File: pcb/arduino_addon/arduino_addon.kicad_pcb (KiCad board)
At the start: 2 copper layers, 100 x 53 mm, 32 parts, among them P1 AnalogIn, P11 ADC-DO, P12 ADC-DO, P13 ADC-DO, P14 ADC-DO, P15 DO, P16 3V3 ADC REF, P2 Power, P3 Digital1, P4 Digital2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

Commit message: adaq initial version, board design: extra bnc connector added
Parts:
- added P17: BNC, rzfp:bnc, F.Cu at (172.0, 113.0)
- P15: footprint Pin_Headers:Pin_Header_Straight_1x05 -> Pin_Headers:Pin_Header_Straight_1x06
- moved D1 29.0 mm to (197.5, 103.2), turned to 180 degrees
- moved R1 7.25 mm to (186.0, 103.2), turned to 0 degrees
- moved C4 6.50 mm to (179.2, 124.2)
- moved R11 6.36 mm to (193.0, 117.2)
- moved P9 5.30 mm to (168.2, 125.2)
- moved R10 4.91 mm to (156.5, 123.2)
- moved R12 4.32 mm to (193.0, 124.2)
- moved R9 3.35 mm to (140.2, 122.5), turned to 180 degrees
- moved P15 2.55 mm to (154.8, 107.5)
- moved C3 0.79 mm to (151.8, 117.0)
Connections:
- P15 pad 1: /D4 -> +3V3
- P15 pad 2: /D5 -> /D4
- P15 pad 3: /D6 -> /D5
- P15 pad 4: /D7 -> /D6
- P15 pad 5: GND -> /D7
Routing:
- net (no net): track 611.8 -> 0.00 mm
- net GND: track 398.9 -> 449.0 mm, vias 5 -> 8
- net +3V3: track 127.2 -> 173.1 mm, vias 1 -> 7
- net /D4: track 5.54 -> 31.9 mm, vias 0 -> 1
- net /AD0: track 42.2 -> 56.6 mm, vias 1 -> 2
- net /D1: track 74.4 -> 63.0 mm, vias 1 -> 2
- net Net-(C3-Pad1): track 33.0 -> 43.5 mm
- net /D8: track 82.6 -> 89.8 mm
- net Net-(R10-Pad1): track 22.4 -> 15.8 mm, vias 1 -> 0
- net /DAC0: track 36.9 -> 30.7 mm
- net /AD2: track 23.6 -> 29.7 mm, vias 0 -> 2
- net /AI2: track 29.8 -> 25.6 mm
- net /D3: track 45.1 -> 48.6 mm
- net Net-(R11-Pad1): track 41.4 -> 44.6 mm
- net /D2: track 54.2 -> 57.1 mm, vias 1 -> 2
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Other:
- net class Default: via_dia 0.7 -> 1.6
- board text added: "BOTTOM"
- board text added: "TOP"

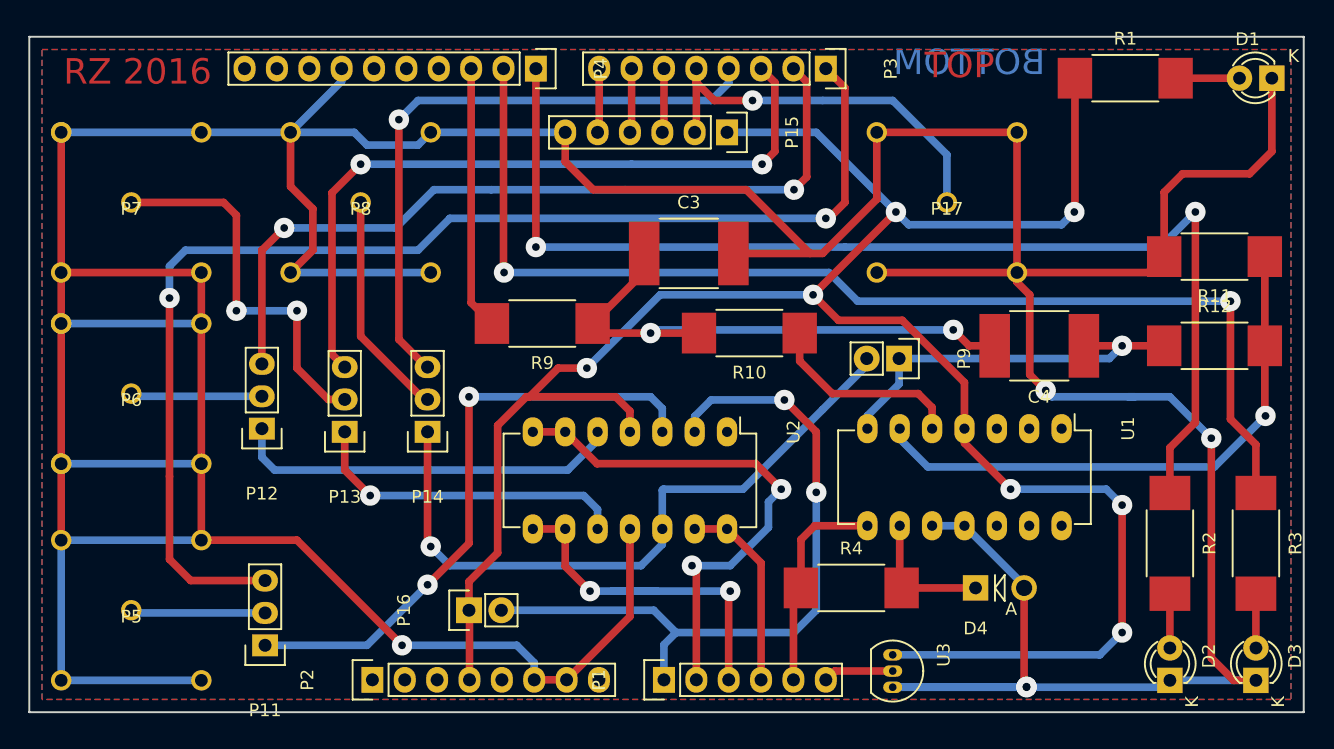
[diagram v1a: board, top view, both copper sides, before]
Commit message: Arduino addon V2 is ready, pmt trig generator firmware is updated
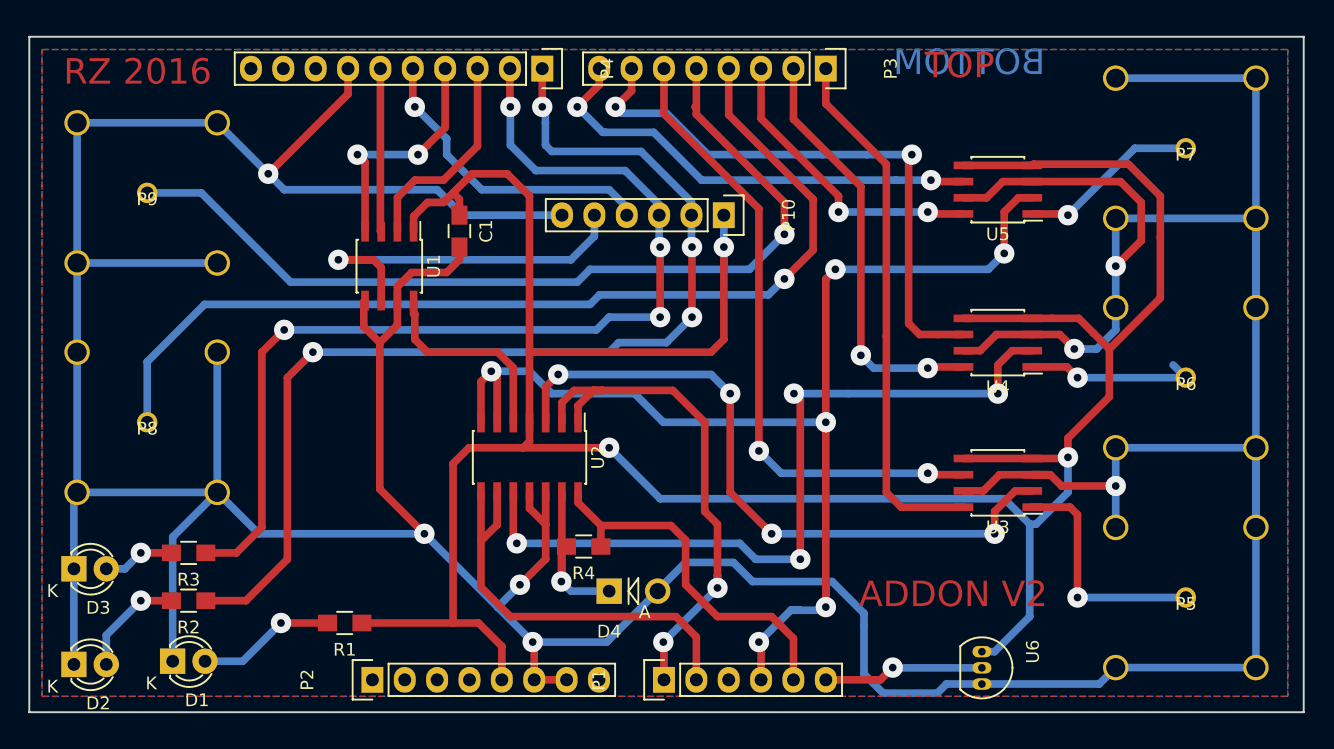
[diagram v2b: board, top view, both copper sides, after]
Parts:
- removed C3, C4: 12n, Capacitors_SMD:C_2220_HandSoldering
- removed P11, P12, P13, P14: ADC-DO, Pin_Headers:Pin_Header_Straight_1x03
- removed P15: DO, Pin_Headers:Pin_Header_Straight_1x06
- removed P16: 3V3 ADC REF, Pin_Headers:Pin_Header_Straight_1x02
- removed P17: BNC, rzfp:bnc
- removed R10, R9: 100k, Resistors_SMD:R_2512_HandSoldering
- removed R11, R12: 10k, Resistors_SMD:R_2512_HandSoldering
- added C1: 100n, Capacitors_SMD:C_0805_HandSoldering, F.Cu at (133.8, 115.2)
- added P10: CONN_01X06, Pin_Headers:Pin_Header_Straight_1x06, F.Cu at (154.5, 114.0)
- added U4: ADG419, Housings_SOIC:SOIC-8_3.9x4.9mm_Pitch1.27mm, F.Cu at (176.0, 124.0)
- added U5: ADG419, Housings_SOIC:SOIC-8_3.9x4.9mm_Pitch1.27mm, F.Cu at (176.0, 112.0)
- added U6: MCP9700T-E/TT, TO_SOT_Packages_THT:TO-92_Inline_Narrow_Oval, F.Cu at (174.8, 148.2)
- P9: value DAC2ADC0 -> BNC; footprint Pin_Headers:Pin_Header_Straight_1x02 -> rzfp:bnc
- R1, R2, R3, R4: footprint Resistors_SMD:R_2512_HandSoldering -> Resistors_SMD:R_0805_HandSoldering
- U1: value LM324 -> MCP4812; footprint Housings_DIP:DIP-14_W7.62mm_LongPads -> Housings_SOIC:SOIC-8_3.9x4.9mm_Pitch1.27mm
- U2: footprint Housings_DIP:DIP-14_W7.62mm_LongPads -> Housings_SOIC:SOIC-14_3.9x8.7mm_Pitch1.27mm
- U3: value MCP9700T-E/TT -> ADG419; footprint TO_SOT_Packages_THT:TO-92_Inline_Narrow_Oval -> Housings_SOIC:SOIC-8_3.9x4.9mm_Pitch1.27mm
- moved D1 97.6 mm to (111.2, 149.0), turned to 0 degrees
- moved D3 93.2 mm to (103.5, 141.8), turned to 0 degrees
- moved D2 86.0 mm to (103.5, 149.2), turned to 0 degrees
- moved R3 83.8 mm to (112.5, 140.5), turned to 180 degrees
- moved P7 82.9 mm to (190.8, 108.8)
- moved P6 82.8 mm to (190.8, 126.8)
- moved P5 82.8 mm to (190.8, 144.0)
- moved R2 77.1 mm to (112.5, 144.2), turned to 180 degrees
- moved R1 74.7 mm to (124.8, 146.0), turned to 180 degrees
- moved P9 60.4 mm to (109.2, 112.2), turned to 0 degrees
- moved U1 54.3 mm to (128.2, 118.0)
- moved D4 28.8 mm to (145.5, 143.5)
- moved P8 24.0 mm to (109.2, 130.2)
- moved R4 21.2 mm to (143.5, 140.0), turned to 180 degrees
- moved U3 15.8 mm to (176.0, 135.0), turned to 180 degrees
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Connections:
- P1 pad 3: /AD2 -> (no net)
- P1 pad 4: /AD3 -> /DAC0
- P2 pad 4: +3V3 -> (no net)
- P2 pad 5: (no net) -> +5V
- P4 pad 4: (no net) -> /D11
- P4 pad 5: (no net) -> /D12
- P4 pad 6: (no net) -> /D13
- P8 pad 1: /BNC3 -> /D3
- P9 pad 1: /DAC0 -> /D4
- P9 pad 2: /AI3 -> GND
- R1 pad 1: +3V3 -> +5V
- U1 pad 1: (no net) -> +5V
- U1 pad 2: (no net) -> /D10
- U1 pad 3: (no net) -> /D13
- U1 pad 4: +3V3 -> /D11
- U1 pad 5: Net-(R10-Pad1) -> GND
- U1 pad 6: Net-(R11-Pad1) -> /DAC1
- U1 pad 7: /DAC0 -> GND
- U1 pad 8: /AD4 -> Net-(U1-Pad8)
- U2 pad 10: /AI2 -> /AI1
- U2 pad 12: /AI3 -> GND
- U2 pad 13: /AD3 -> Net-(D4-Pad1)
- U2 pad 14: /AD3 -> /AD4
- U2 pad 4: +3V3 -> +5V
- U2 pad 5: /AI1 -> Net-(U1-Pad8)
- U2 pad 6: /AD1 -> /DAC0
- U2 pad 7: /AD1 -> /DAC0
- U2 pad 8: /AD2 -> /AD1
- U2 pad 9: /AD2 -> /AD1
- U3 pad 1: +3V3 -> /BNC0
- U3 pad 2: /AD5 -> /AI0
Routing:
- net +5V: track 0.00 -> 216.0 mm, vias 0 -> 3
- net +3V3: track 173.1 -> 0.00 mm, vias 7 -> 0
- net /DAC0: track 30.7 -> 93.7 mm, vias 1 -> 6
- net /D0: track 97.4 -> 41.7 mm, vias 2 -> 0
- net /AI3: track 53.5 -> 0.00 mm, vias 1 -> 0
- net /D5: track 5.05 -> 49.9 mm, vias 0 -> 2
- net Net-(R11-Pad1): track 44.6 -> 0.00 mm, vias 1 -> 0
- net Net-(C3-Pad1): track 43.5 -> 0.00 mm, vias 2 -> 0
- net /D6: track 5.05 -> 47.1 mm, vias 0 -> 2
- net /D4: track 31.9 -> 70.4 mm
- net /D2: track 57.1 -> 23.6 mm
- net /D7: track 5.05 -> 37.0 mm, vias 0 -> 2
- net /AI1: track 30.6 -> 61.5 mm, vias 0 -> 4
- net /D1: track 63.0 -> 33.2 mm
- net /AD2: track 29.7 -> 0.00 mm, vias 2 -> 0
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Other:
- board text added: "ADDON V2"
